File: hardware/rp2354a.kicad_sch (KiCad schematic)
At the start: 15 parts, among them U1 RP2354A

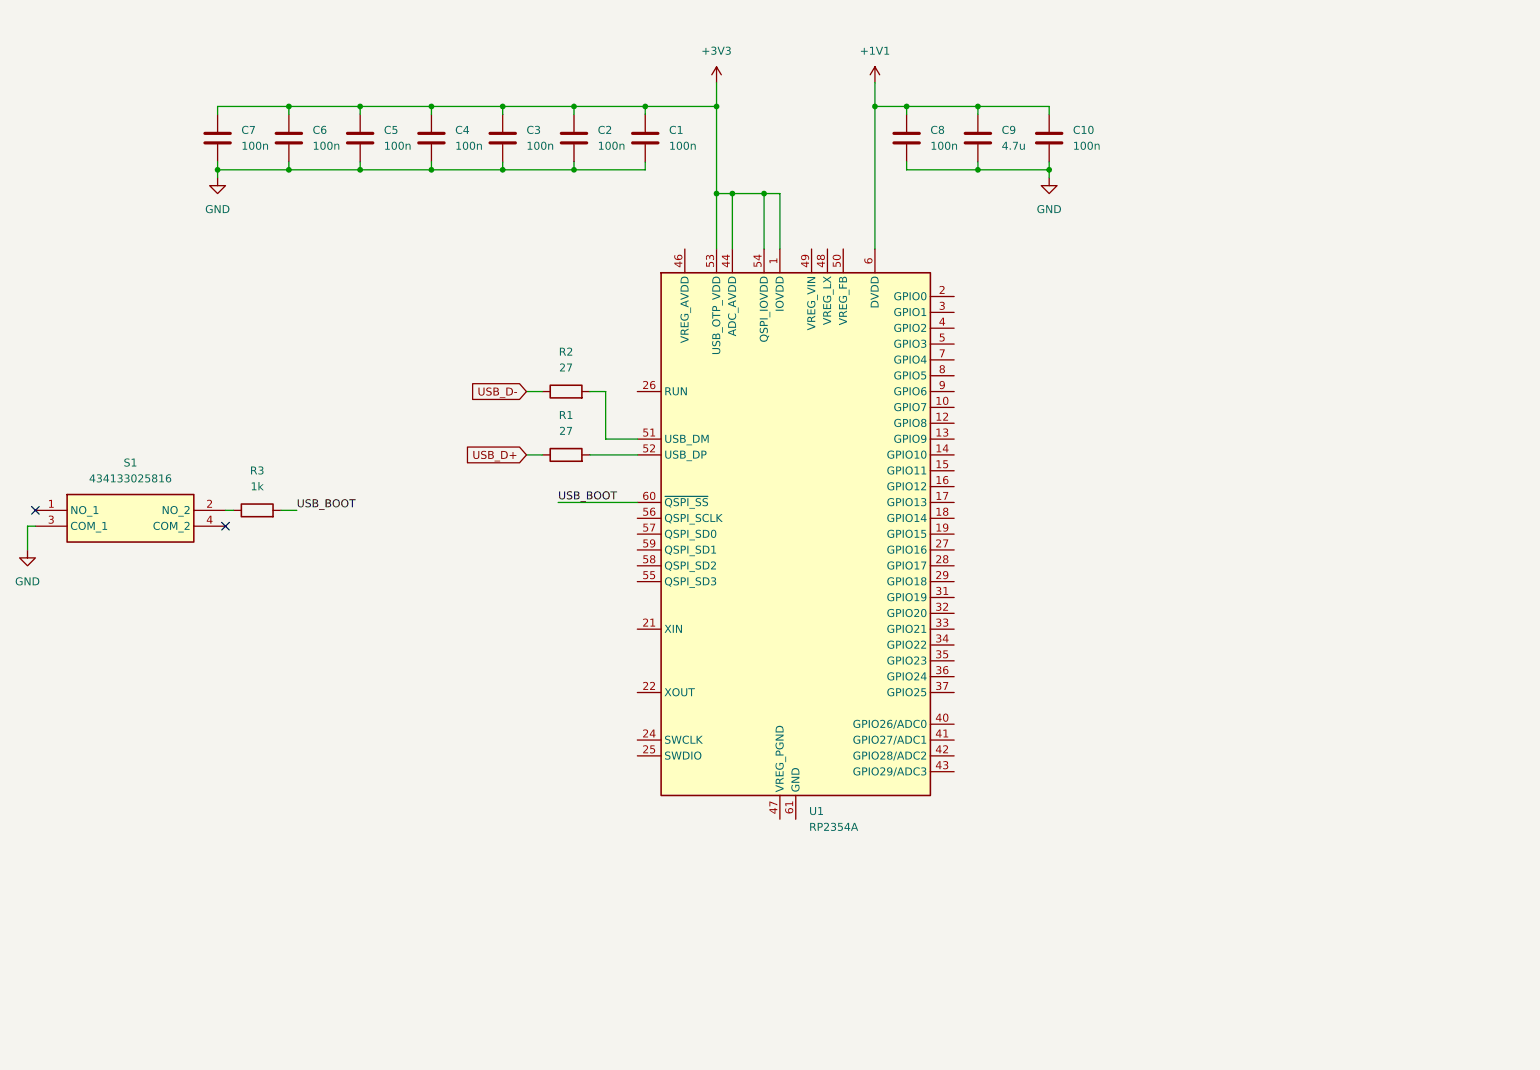
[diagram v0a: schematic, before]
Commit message: Most RP components on board. Core regulator wired up
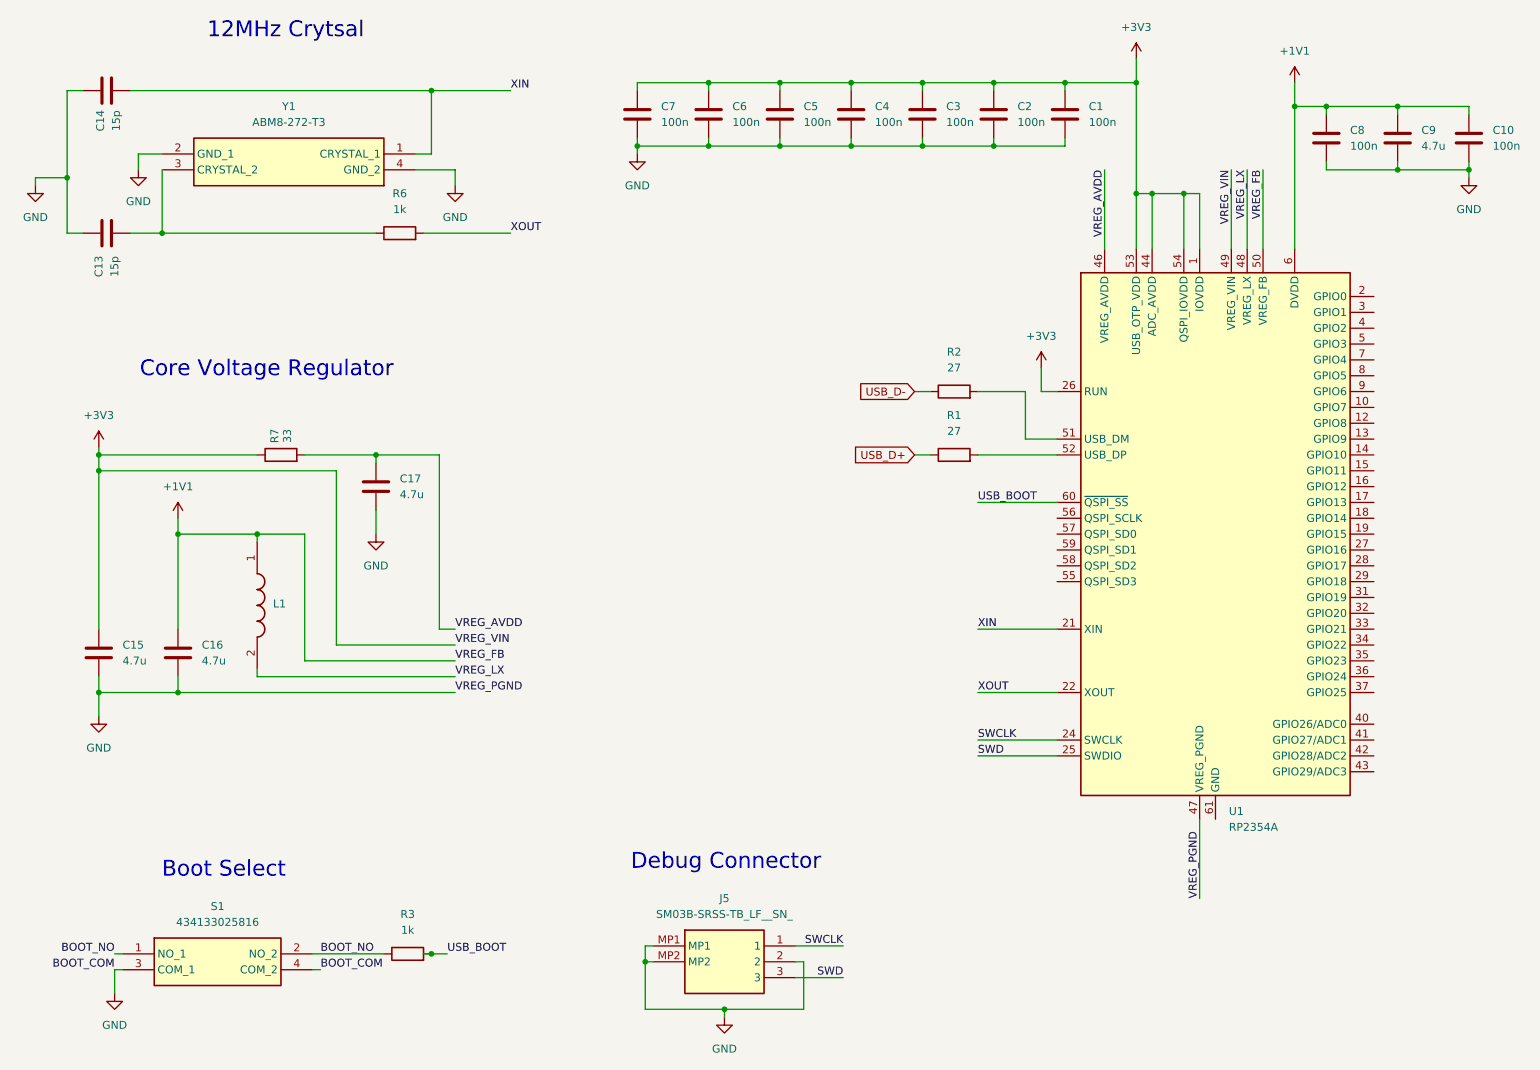
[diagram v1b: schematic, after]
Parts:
- added C13, C14: 15p, Capacitor_SMD:C_0402_1005Metric, symbol Device:C
- added C15, C16: 4.7u, Stuttgart:C_0402_1005Metric_small_pads, symbol Device:C
- added C17: 4.7u, Capacitor_SMD:C_0402_1005Metric, symbol Device:C
- added J5: SM03B-SRSS-TB_LF__SN_, Stuttgart:SM03BSRSSTBLFSN, symbol Stuttgart:SM03B-SRSS-TB_LF__SN_
- added L1: AOTA-B201610S3R3-101-T, Stuttgart:AOTAB201610S3R3101T, symbol Stuttgart:AOTA-B201610S3R3-101-T
- added R6: 1k, Resistor_SMD:R_0402_1005Metric, symbol Device:R
- added R7: 33, Resistor_SMD:R_0402_1005Metric, symbol Device:R
- added Y1: ABM8-272-T3, Stuttgart:ABM8272T3, symbol Stuttgart:ABM8-272-T3
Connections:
- net +1V1: now also U1.50 (VREG_FB), C16.1, L1.1
- net +3V3: now also U1.26 (RUN), U1.49 (VREG_VIN), C15.1, R7.1
- net GND: now also S1.4 (COM_2), U1.47 (VREG_PGND), C13.2, C14.1, C15.2, C16.2, C17.2, J5.2, J5.MP1, J5.MP2, Y1.2 (GND_1), Y1.4 (GND_2)
- net XIN: now reaches U1.21 (XIN)
- net XIN: now also C14.2, Y1.1 (CRYSTAL_1)
- net XOUT: now reaches U1.22 (XOUT)
- net XOUT: now also R6.2
- net SWCLK: now reaches U1.24 (SWCLK)
- net SWCLK: now also J5.1
- net SWD: now reaches U1.25 (SWDIO)
- net SWD: now also J5.3
- net VREG_AVDD: now reaches U1.46 (VREG_AVDD)
- net VREG_AVDD: now also C17.1, R7.2
- net VREG_LX: now reaches U1.48 (VREG_LX)
- net VREG_LX: now also L1.2
- net BOOT_NO: now reaches R3.1, S1.2 (NO_2)
- net BOOT_NO: now also S1.1 (NO_1)
- new net: C13.1, R6.1, Y1.3 (CRYSTAL_2)
- no-connect marks 2 -> 0
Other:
- note added: "12MHz Crytsal"
- note added: "Boot Select"
- note added: "Core Voltage Regulator"
- note added: "Debug Connector"
- moved on the sheet: C1, C10, C2, C3, C4, C5, C6, C7, C8, C9, R1, R2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

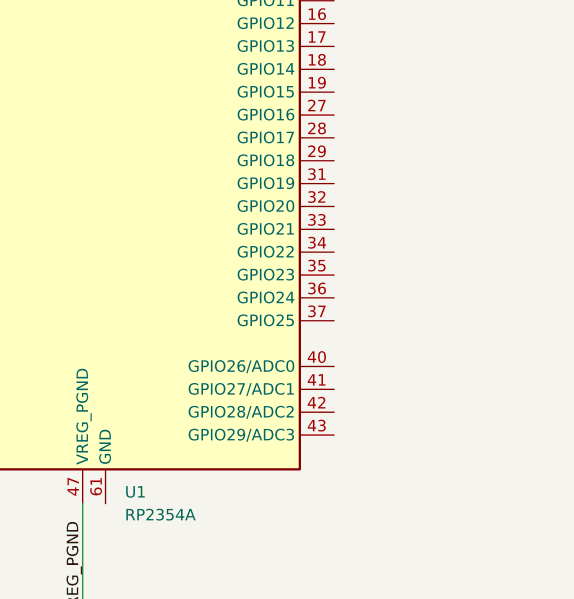
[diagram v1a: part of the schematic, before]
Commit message: Wired in RP Crystal
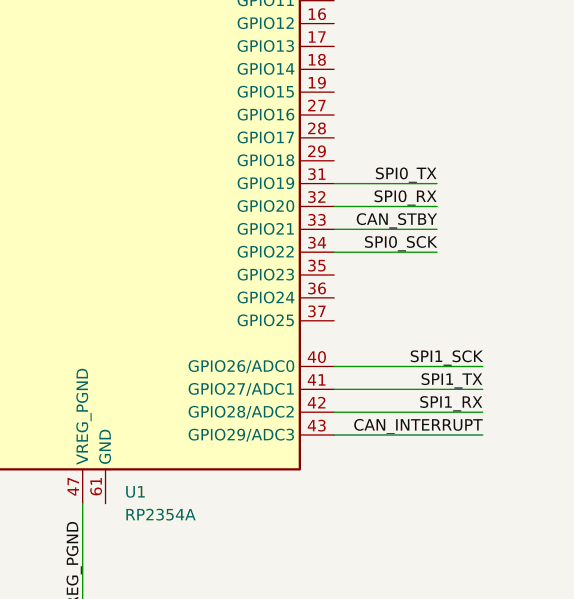
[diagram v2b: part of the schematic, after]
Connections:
- net SPI0_TX: now reaches U1.31 (GPIO19)
- net SPI0_RX: now reaches U1.32 (GPIO20)
- net CAN_STBY: now reaches U1.33 (GPIO21)
- net SPI0_SCK: now reaches U1.34 (GPIO22)
- net SPI1_SCK: now reaches U1.40 (GPIO26/ADC0)
- net SPI1_TX: now reaches U1.41 (GPIO27/ADC1)
- net SPI1_RX: now reaches U1.42 (GPIO28/ADC2)
- net CAN_INTERRUPT: now reaches U1.43 (GPIO29/ADC3)
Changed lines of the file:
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@@
+	(wire
+		(pts
+			(xy 238.76 132.08) (xy 255.27 132.08)
+		)
+		(stroke
+			(width 0)
+			(type default)
+		)
+	)
 	(wire
 		(pts
@@
 	(wire
 		(pts
+			(xy 238.76 116.84) (xy 250.19 116.84)
+		)
+		(stroke
+			(width 0)
+			(type default)
+		)
+	)
+	(wire
+		(pts
 			(xy 175.26 88.9) (xy 187.96 88.9)
 		)
@@
 	(wire
 		(pts
+			(xy 238.76 139.7) (xy 255.27 139.7)
+		)
+		(stroke
+			(width 0)
+			(type default)
+		)
+	)
+	(wire
+		(pts
 			(xy 91.44 127) (xy 46.99 127)
 		)
@@
 	(wire
 		(pts
+			(xy 238.76 114.3) (xy 250.19 114.3)
+		)
+		(stroke
+			(width 0)
+			(type default)
+		)
+	)
+	(wire
+		(pts
 			(xy 40.64 40.64) (xy 44.45 40.64)
 		)
@@
 	(wire
 		(pts
+			(xy 238.76 119.38) (xy 250.19 119.38)
+		)
+		(stroke
+			(width 0)
+			(type default)
+		)
+	)
+	(wire
+		(pts
 			(xy 146.05 167.64) (xy 153.67 167.64)
 		)
@@
 	(wire
 		(pts
+			(xy 238.76 137.16) (xy 255.27 137.16)
+		)
+		(stroke
+			(width 0)
+			(type default)
+		)
+	)
+	(wire
+		(pts
 			(xy 182.88 86.36) (xy 182.88 78.74)
 		)
@@
 	(wire
 		(pts
+			(xy 238.76 111.76) (xy 250.19 111.76)
+		)
+		(stroke
+			(width 0)
+			(type default)
+		)
+	)
+	(wire
+		(pts
 			(xy 68.58 168.91) (xy 80.01 168.91)
 		)
@@
 		(pts
 			(xy 143.51 39.37) (xy 154.94 39.37)
+		)
+		(stroke
+			(width 0)
+			(type default)
+		)
+	)
+	(wire
+		(pts
+			(xy 238.76 134.62) (xy 255.27 134.62)
 		)
 		(stroke
@@
 		)
 	)
+	(label "SPI0_TX"
+		(at 250.19 111.76 180)
+		(effects
+			(font
+				(size 1.27 1.27)
+			)
+			(justify right bottom)
+		)
+	)
 	(label "VREG_AVDD"
 		(at 195.58 43.18 270)
@@
 		)
 	)
+	(label "SPI0_RX"
+		(at 250.19 114.3 180)
+		(effects
+			(font
+				(size 1.27 1.27)
+			)
+			(justify right bottom)
+		)
+	)
+	(label "CAN_STBY"
+		(at 250.19 116.84 180)
+		(effects
+			(font
+				(size 1.27 1.27)
+			)
+			(justify right bottom)
+		)
+	)
 	(label "XIN"
 		(at 175.26 116.84 0)
@@
 		)
 	)
+	(label "SPI1_SCK"
+		(at 255.27 132.08 180)
+		(effects
+			(font
+				(size 1.27 1.27)
+			)
+			(justify right bottom)
+		)
+	)
+	(label "SPI0_SCK"
+		(at 250.19 119.38 180)
+		(effects
+			(font
+				(size 1.27 1.27)
+			)
+			(justify right bottom)
+		)
+	)
+	(label "SPI1_TX"
+		(at 255.27 134.62 180)
+		(effects
+			(font
+				(size 1.27 1.27)
+			)
+			(justify right bottom)
+		)
+	)
+	(label "SPI1_RX"
+		(at 255.27 137.16 180)
+		(effects
+			(font
+				(size 1.27 1.27)
+			)
+			(justify right bottom)
+		)
+	)
 	(label "BOOT_NO"
 		(at 69.85 168.91 0)
@@
 		(effects
 			(font
+				(size 1.27 1.27)
+			)
+			(justify right bottom)
+		)
+	)
+	(label "CAN_INTERRUPT"
+		(at 255.27 139.7 180)
+		(effects
+			(font

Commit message: Further RP development - Kicad keeps crashing
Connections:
- net GND: now also U1.61 (GND)
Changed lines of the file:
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@@
 	(wire
 		(pts
+			(xy 213.36 147.32) (xy 213.36 148.59)
+		)
+		(stroke
+			(width 0)
+			(type default)
+		)
+	)
+	(wire
+		(pts
 			(xy 134.62 177.8) (xy 121.92 177.8)
 		)
@@
 					(unit 1)
 				)
+			)
+		)
+	)
+	(symbol
+		(lib_id "power:GND")
+		(at 213.36 148.59 0)
+		(unit 1)
+		(body_style 1)
+		(exclude_from_sim no)
+		(in_bom yes)
+		(on_board yes)
+		(in_pos_files yes)
+		(dnp no)
+		(fields_autoplaced yes)
+		(property "Reference" "#PWR023"
+			(at 213.36 154.94 0)
+			(hide yes)
+			(show_name no)
+			(do_not_autoplace no)
+			(effects
+				(font
+					(size 1.27 1.27)
+				)
+			)
+		)
+		(property "Value" "GND"
+			(at 213.36 153.67 0)
+			(show_name no)
+			(do_not_autoplace no)
+			(effects
+				(font
+					(size 1.27 1.27)
+				)
+			)
+		)
+		(property "Footprint" ""
+			(at 213.36 148.59 0)
+			(hide yes)
+			(show_name no)
+			(do_not_autoplace no)
+			(effects
+				(font
+					(size 1.27 1.27)
+				)
+			)
+		)
+		(property "Datasheet" ""
+			(at 213.36 148.59 0)
+			(hide yes)
+			(show_name no)
+			(do_not_autoplace no)
+			(effects
+				(font
+					(size 1.27 1.27)
+				)
+			)
+		)
+		(property "Description" "Power symbol creates a global label with name \"GND\" , ground"
+			(at 213.36 148.59 0)
+			(hide yes)
+			(show_name no)
+			(do_not_autoplace no)
+			(effects
+				(font
+					(size 1.27 1.27)
+				)
+			)
+		)
+		(pin "1"
+		)
+		(instances
+			(project "Stuttgart"
+				(path "/6d354744-ce95-4d5c-b7ae-1990dae66f7b/1e03cc0a-6ff0-4ffa-8c67-8bd6ffc32d81"
+					(reference "#PWR023")
+					(unit 1)
+				)

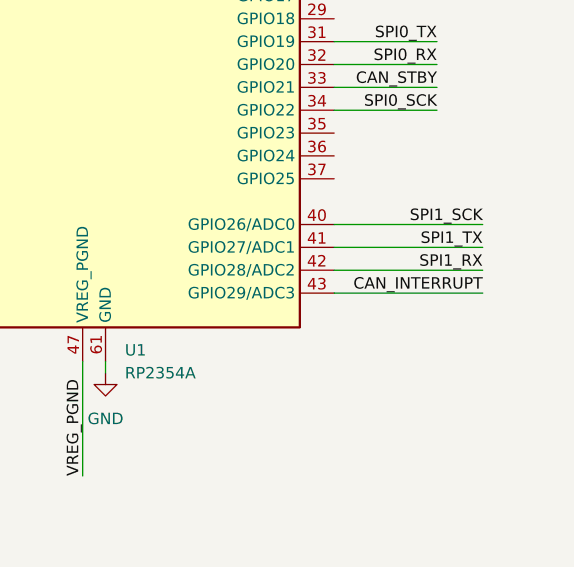
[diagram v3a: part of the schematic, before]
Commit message: Core RP pad work complete
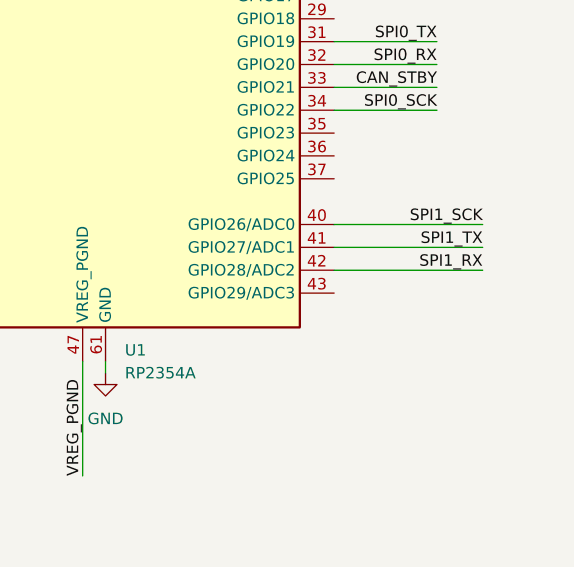
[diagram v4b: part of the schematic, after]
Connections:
- net CAN_INTERRUPT: no longer names the net of U1.43 (GPIO29/ADC3)
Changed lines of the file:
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@@
-	(wire
-		(pts
-			(xy 238.76 139.7) (xy 255.27 139.7)
-		)
-		(stroke
-			(width 0)
-			(type default)
-		)
-	)
 	(wire
 		(pts
@@
 		(effects
 			(font
-				(size 1.27 1.27)
-			)
-			(justify right bottom)
-		)
-	)
-	(label "CAN_INTERRUPT"
-		(at 255.27 139.7 180)
-		(effects
-			(font

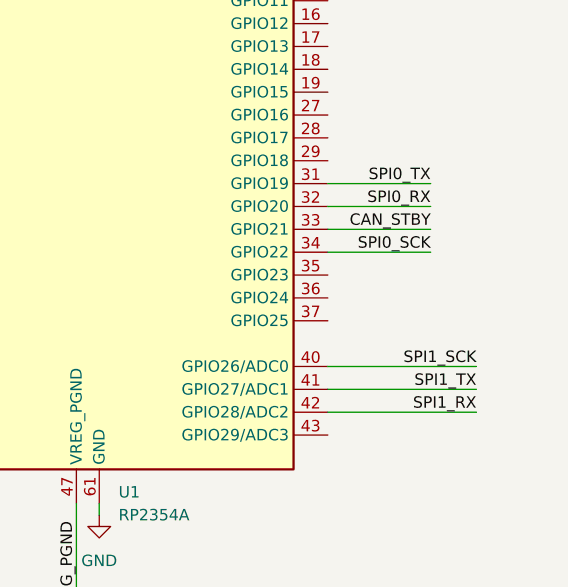
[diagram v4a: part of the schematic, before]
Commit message: Isolation bridges complete
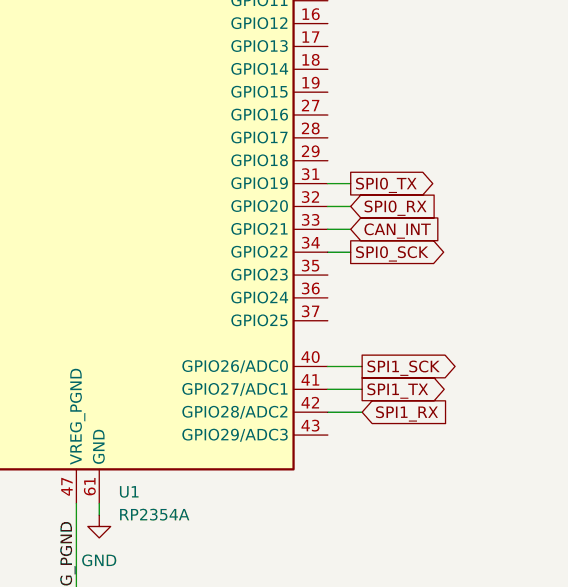
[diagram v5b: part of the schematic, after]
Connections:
- net CAN_STBY renamed CAN_INT
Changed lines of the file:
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@@
 	(wire
 		(pts
-			(xy 238.76 132.08) (xy 255.27 132.08)
+			(xy 238.76 132.08) (xy 242.57 132.08)
 		)
 		(stroke
@@
 	(wire
 		(pts
-			(xy 238.76 116.84) (xy 250.19 116.84)
+			(xy 238.76 116.84) (xy 241.3 116.84)
 		)
 		(stroke
@@
 	(wire
 		(pts
-			(xy 238.76 114.3) (xy 250.19 114.3)
+			(xy 238.76 114.3) (xy 241.3 114.3)
 		)
 		(stroke
@@
 	(wire
 		(pts
-			(xy 238.76 119.38) (xy 250.19 119.38)
+			(xy 238.76 119.38) (xy 241.3 119.38)
 		)
 		(stroke
@@
 	(wire
 		(pts
-			(xy 238.76 137.16) (xy 255.27 137.16)
+			(xy 238.76 137.16) (xy 242.57 137.16)
 		)
 		(stroke
@@
 	(wire
 		(pts
-			(xy 238.76 111.76) (xy 250.19 111.76)
+			(xy 238.76 111.76) (xy 241.3 111.76)
 		)
 		(stroke
@@
 	(wire
 		(pts
-			(xy 238.76 134.62) (xy 255.27 134.62)
+			(xy 238.76 134.62) (xy 242.57 134.62)
 		)
 		(stroke
@@
 		)
 	)
-	(label "SPI0_TX"
-		(at 250.19 111.76 180)
-		(effects
-			(font
-				(size 1.27 1.27)
-			)
-			(justify right bottom)
-		)
-	)
 	(label "VREG_AVDD"
 		(at 195.58 43.18 270)
@@
 		)
 	)
-	(label "SPI0_RX"
-		(at 250.19 114.3 180)
-		(effects
-			(font
-				(size 1.27 1.27)
-			)
-			(justify right bottom)
-		)
-	)
-	(label "CAN_STBY"
-		(at 250.19 116.84 180)
-		(effects
-			(font
-				(size 1.27 1.27)
-			)
-			(justify right bottom)
-		)
-	)
 	(label "XIN"
 		(at 175.26 116.84 0)
@@
 			)
 			(justify left bottom)
-		)
-	)
-	(label "SPI1_SCK"
-		(at 255.27 132.08 180)
-		(effects
-			(font
-				(size 1.27 1.27)
-			)
-			(justify right bottom)
-		)
-	)
-	(label "SPI0_SCK"
-		(at 250.19 119.38 180)
-		(effects
-			(font
-				(size 1.27 1.27)
-			)
-			(justify right bottom)
-		)
-	)
-	(label "SPI1_TX"
-		(at 255.27 134.62 180)
-		(effects
-			(font
-				(size 1.27 1.27)
-			)
-			(justify right bottom)
-		)
-	)
-	(label "SPI1_RX"
-		(at 255.27 137.16 180)
-		(effects
-			(font
-				(size 1.27 1.27)
-			)
-			(justify right bottom)
 		)
 	)
@@
 		)
 	)
+	(global_label "SPI0_RX"
+		(shape input)
+		(at 241.3 114.3 0)
+		(fields_autoplaced yes)
+		(effects
+			(font
+				(size 1.27 1.27)
+			)
+			(justify left)
+		)
+		(property "Intersheetrefs" "${INTERSHEET_REFS}"
+			(at 252.0261 114.3 0)
+			(hide yes)
+			(show_name no)
+			(do_not_autoplace no)
+			(effects
+				(font
+					(size 1.27 1.27)
+				)
+				(justify left)
+			)
+		)
+	)
+	(global_label "SPI1_RX"
+		(shape input)
+		(at 242.57 137.16 0)
+		(fields_autoplaced yes)
+		(effects
+			(font
+				(size 1.27 1.27)
+			)
+			(justify left)
+		)
+		(property "Intersheetrefs" "${INTERSHEET_REFS}"
+			(at 253.2961 137.16 0)
+			(hide yes)
+			(show_name no)
+			(do_not_autoplace no)
+			(effects
+				(font
+					(size 1.27 1.27)
+				)
+				(justify left)
+			)
+		)
+	)
+	(global_label "SPI1_SCK"
+		(shape output)
+		(at 242.57 132.08 0)
+		(fields_autoplaced yes)
+		(effects
+			(font
+				(size 1.27 1.27)
+			)
+			(justify left)
+		)
+		(property "Intersheetrefs" "${INTERSHEET_REFS}"
+			(at 254.5661 132.08 0)
+			(hide yes)
+			(show_name no)
+			(do_not_autoplace no)
+			(effects
+				(font
+					(size 1.27 1.27)
+				)
+				(justify left)
+			)
+		)
+	)
 	(global_label "USB_D+"
 		(shape input)
@@
 			)
 		)
+	)
+	(global_label "SPI1_TX"
+		(shape output)
+		(at 242.57 134.62 0)
+		(fields_autoplaced yes)
+		(effects
+			(font
+				(size 1.27 1.27)
+			)
+			(justify left)
+		)
+		(property "Intersheetrefs" "${INTERSHEET_REFS}"
+			(at 252.9937 134.62 0)
+			(hide yes)
+			(show_name no)
+			(do_not_autoplace no)
+			(effects
+				(font
+					(size 1.27 1.27)
+				)
+				(justify left)
+			)
+		)
+	)
+	(global_label "CAN_INT"
+		(shape input)
+		(at 241.3 116.84 0)
+		(fields_autoplaced yes)
+		(effects
+			(font
+				(size 1.27 1.27)
+			)
+			(justify left)
+		)
+		(property "Intersheetrefs" "${INTERSHEET_REFS}"
+			(at 251.8448 116.84 0)
+			(hide yes)
+			(show_name no)
+			(do_not_autoplace no)
+			(effects
+				(font
+					(size 1.27 1.27)
+				)
+				(justify left)
+			)
+		)
+	)
+	(global_label "SPI0_TX"
+		(shape output)
+		(at 241.3 111.76 0)
+		(fields_autoplaced yes)
+		(effects
+			(font
+				(size 1.27 1.27)
+			)
+			(justify left)
+		)
+		(property "Intersheetrefs" "${INTERSHEET_REFS}"
+			(at 251.7237 111.76 0)
+			(hide yes)
+			(show_name no)
+			(do_not_autoplace no)
+			(effects
+				(font
+					(size 1.27 1.27)
+				)
+				(justify left)
+			)
+		)
+	)
+	(global_label "SPI0_SCK"
+		(shape output)
+		(at 241.3 119.38 0)
+		(fields_autoplaced yes)
+		(effects
+			(font
+				(size 1.27 1.27)
+			)
+			(justify left)
+		)
+		(property "Intersheetrefs" "${INTERSHEET_REFS}"
+			(at 253.2961 119.38 0)
+			(hide yes)
+			(show_name no)
+			(do_not_autoplace no)
+			(effects
+				(font
+					(size 1.27 1.27)
+				)
+				(justify left)
+			)
+		)
